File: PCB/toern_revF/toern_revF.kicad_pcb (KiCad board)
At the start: 4 copper layers, 160 x 71 mm, 92 parts, among them J1 AudioJack3_Switch, J10 Conn_01x02, J11 Conn_01x05, J11.5 Conn_01x05, J12 Conn_01x05, J13 Conn_01x05, J14 Conn_01x05, J15 Conn_01x05, J16 BATTERY, J17 AudioJack3_Ground, J3 AudioJack3_Ground, J4 USB_C_Receptacle_USB2.0, J5 AudioJack3_Switch, J6 AudioJack3_Switch, J7 AudioJack3_Switch, J8 Micro_SD_Card, J9 Conn_01x03, Q1 DMG3415, SW1 EG2219, U1 SPX3819M5-L-3-3, U10 01x05 Connector_PinSocket_2.5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, U11 01x05 Connector_PinSocket_2.5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, U12 01x05 Connector_PinSocket_2.5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, U13 PAM8403D, U2 SPX3819M5-L-1-8, U3 SGTL5000XNBA3, U4 TLP2361V4_E, U5 74LVC2G14, U6 Teensy4.1, U7 SPX3819M5-L-3-3, U8 MCP73831-3-OT, U9 01x05 Connector_PinSocket_2.5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

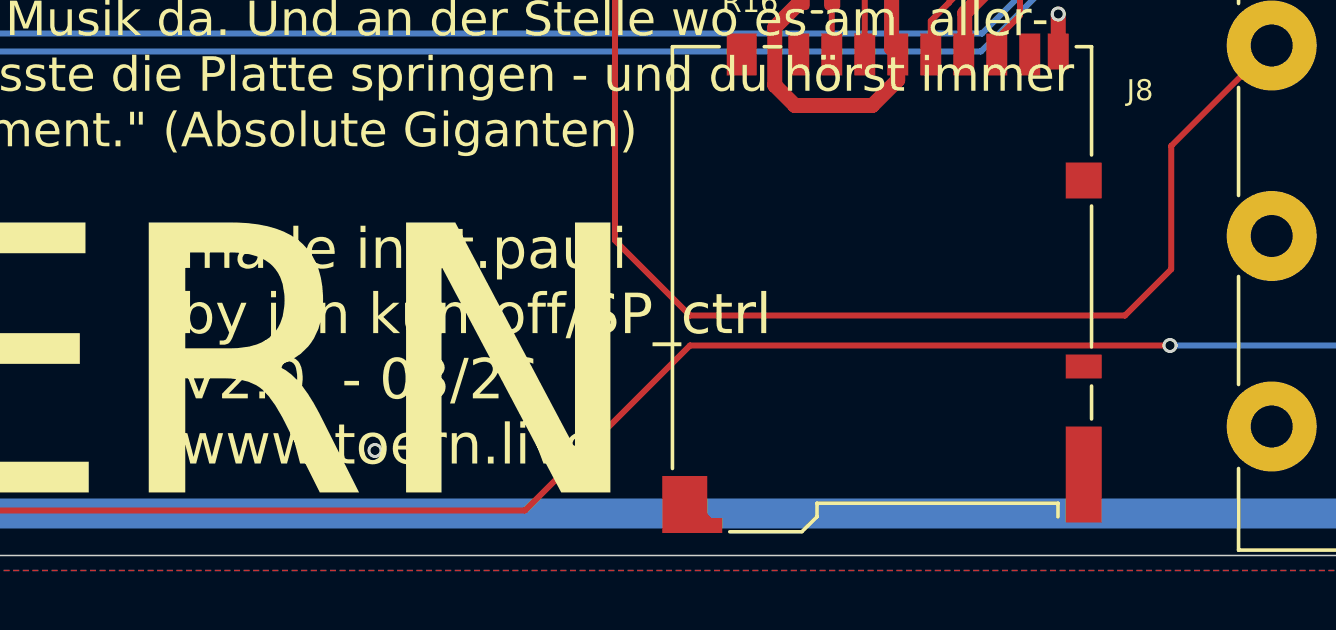
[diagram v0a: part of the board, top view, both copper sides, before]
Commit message: fixed audio/pack loading and handling, also added eyes screensaver
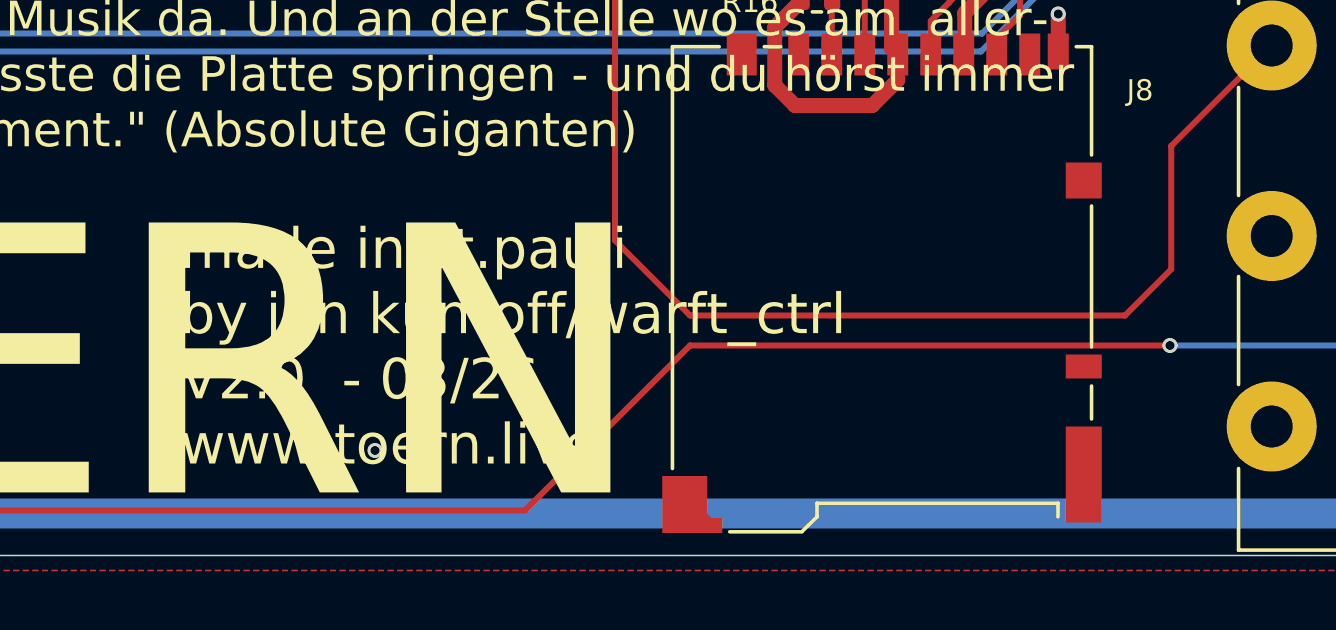
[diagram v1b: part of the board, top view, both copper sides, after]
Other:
- board text added: "made in st.pauli by jan kuntoff/warft_ctrl V2.0 - 03/26 www.toern.live"
- board text removed: "made in st.pauli by jan kuntoff/SP_ctrl V2.0 - 03/26 www.toern.live"
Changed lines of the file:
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@@
 		)
 	)
-	(gr_text "made in st.pauli \nby jan kuntoff/SP_ctrl\nV2.0  - 03/26\nwww.toern.live\n"
+	(gr_text "made in st.pauli \nby jan kuntoff/warft_ctrl\nV2.0  - 03/26\nwww.toern.live\n"
 		(at 97.5 85 0)
 		(layer "F.SilkS")
@@
 			(justify left top)
 		)
-		(render_cache "made in st.pauli \nby jan kuntoff/SP_ctrl\nV2.0  - 03/26\nwww.toern.live\n"
+		(render_cache "made in st.pauli \nby jan kuntoff/warft_ctrl\nV2.0  - 03/26\nwww.toern.live\n"
 			0
 			(polygon
